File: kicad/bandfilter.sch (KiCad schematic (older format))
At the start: 102 parts, among them J1 Antenna, J2 Rx, J3 Tx, J4 Conn_01x07, J5 Conn_01x07, J6 Antenna, J7 Rx, J8 Tx, T1 40/13T T50-2 (8uH), T2 30/8T T50-2 (4.5uH)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

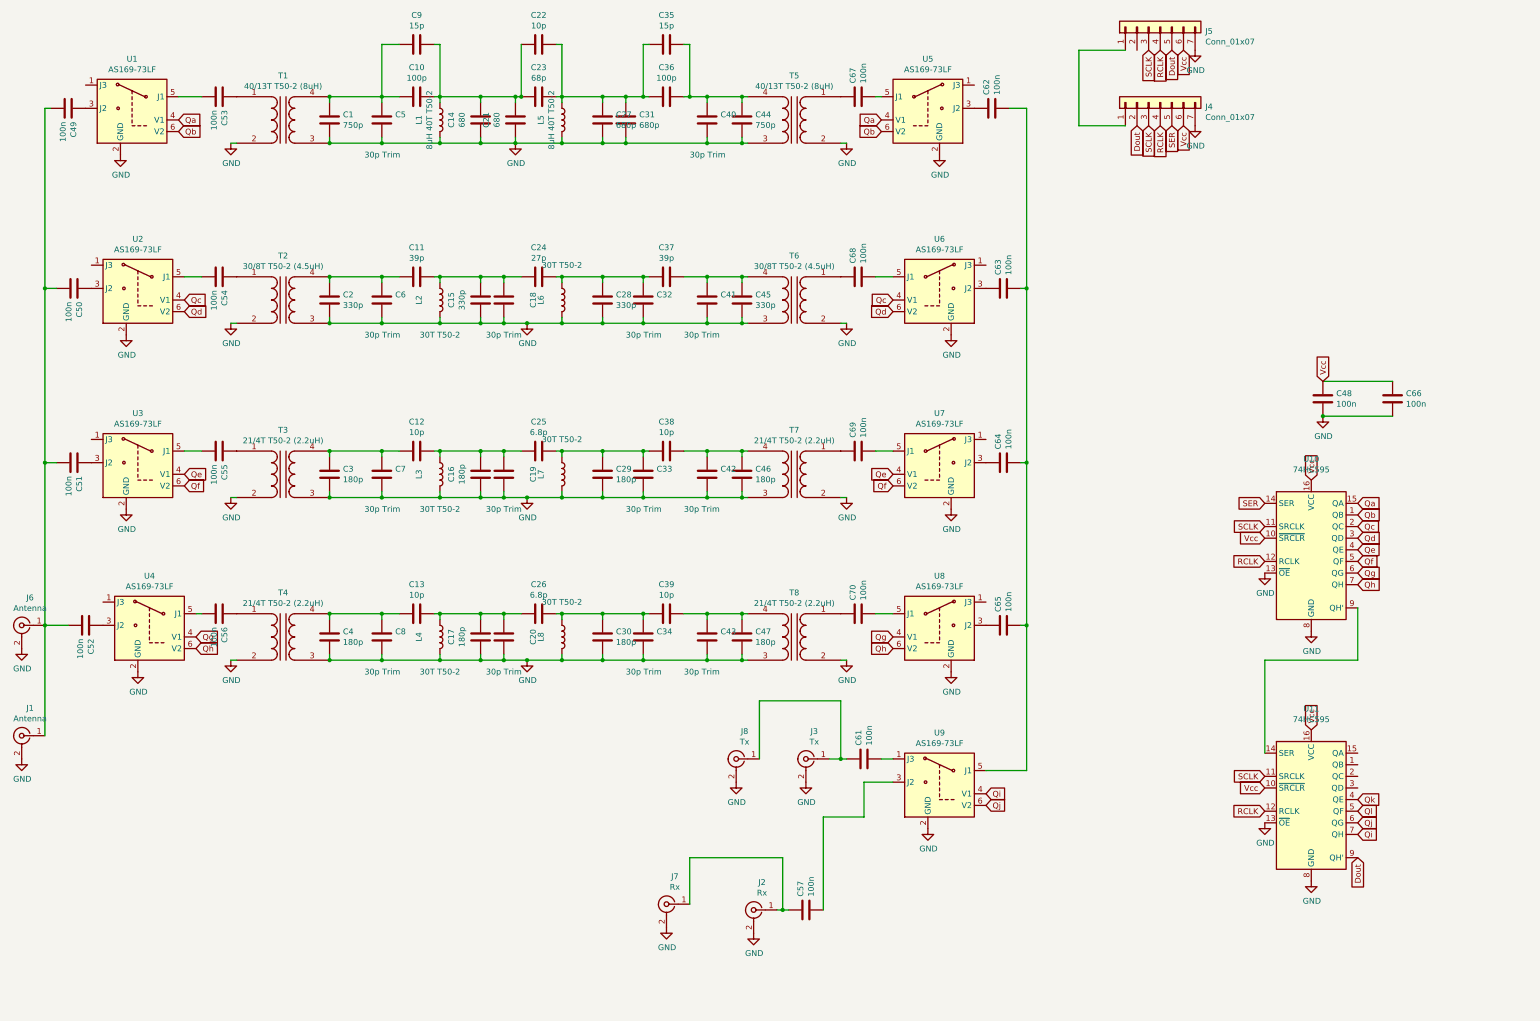
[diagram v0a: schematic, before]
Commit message: I2C version update
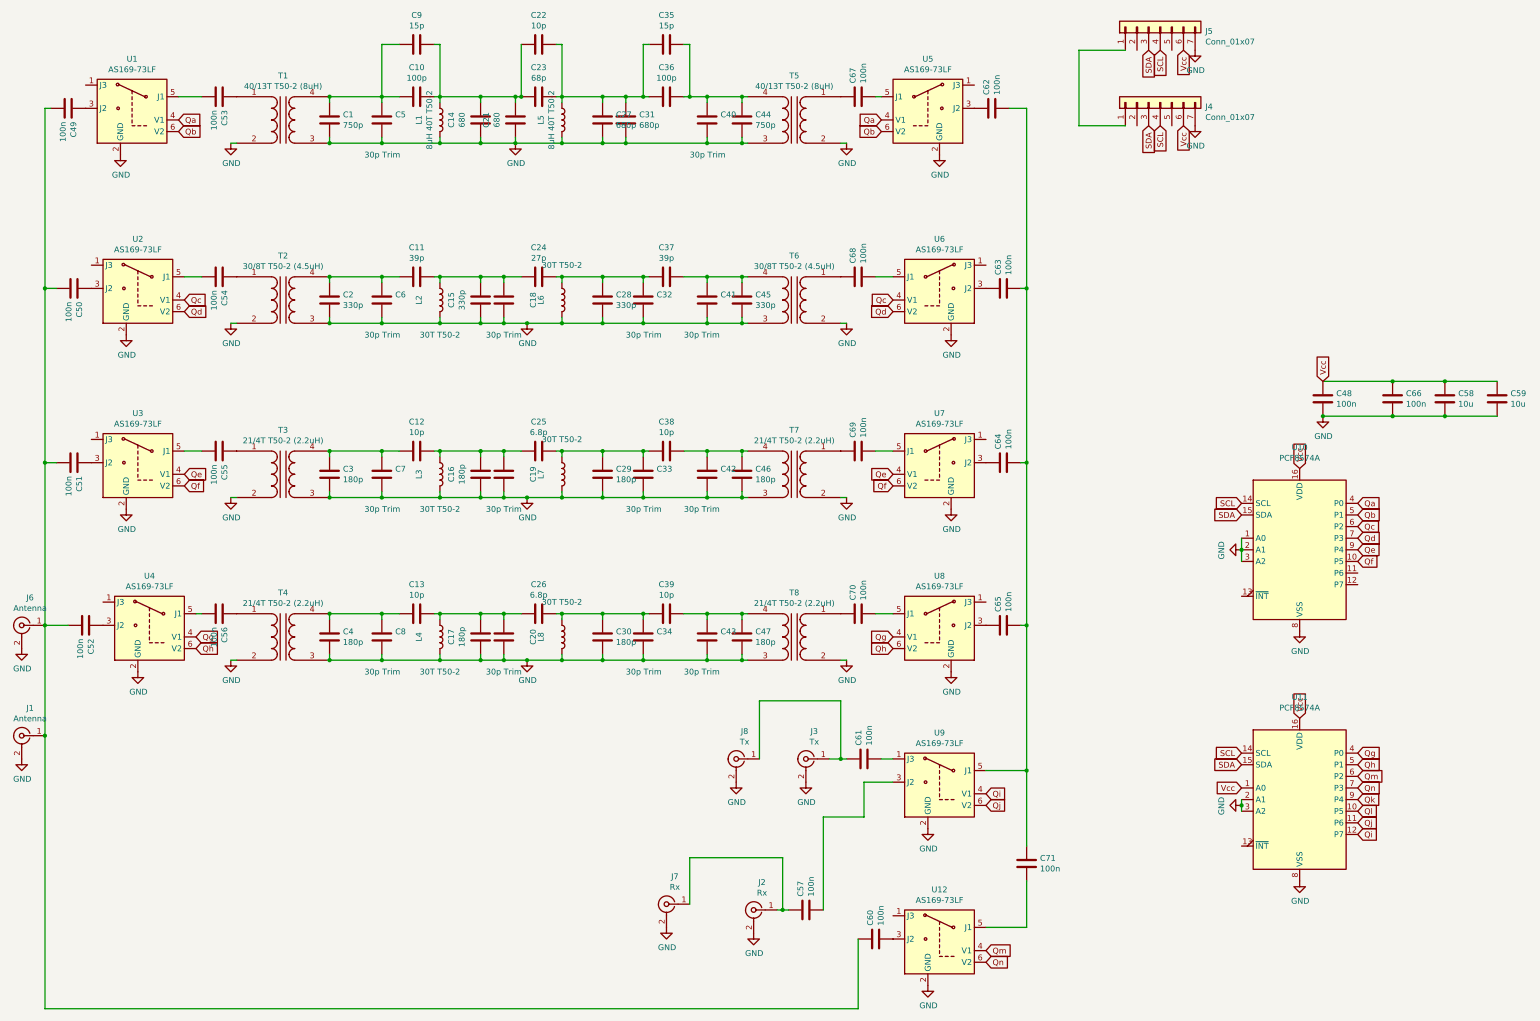
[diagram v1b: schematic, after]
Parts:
- removed U10, U11: 74HC595, Package_DIP:DIP-16_W7.62mm_Socket, symbol 74xx:74HC595
- added C58, C59: 10u, Capacitor_SMD:C_1206_3216Metric_Pad1.42x1.75mm_HandSolder, symbol Device:C
- added C60, C71: 100n, Capacitor_SMD:C_1206_3216Metric_Pad1.42x1.75mm_HandSolder, symbol Device:C
- added U10, U11: PCF8574A, Package_SO:SOP-16_7.5x10.4mm_P1.27mm, symbol Interface_Expansion:PCF8574A
- added U12: AS169-73LF, Package_TO_SOT_SMD:SOT-23-6_Handsoldering, symbol bandfilter-rescue:AS169-73LF-RF_Switch
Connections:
- net GND: now also C58.1, C59.1, U10.1 (A0), U10.2 (A1), U10.3 (A2), U10.8 (VSS), U11.2 (A1), U11.3 (A2), U11.8 (VSS), U12.2 (GND)
- net Qa: now also U10.4 (P0)
- net Qb: now also U10.5 (P1)
- net Qc: now also U10.6 (P2)
- net Qd: now also U10.7 (P3)
- net Qe: now also U10.9 (P4)
- net Qf: now also U10.10 (P5)
- net Qg: now also U11.4 (P0)
- net Qh: now also U11.5 (P1)
- net Qi: now also U11.12 (P7)
- net Qj: now also U11.11 (P6)
- net Qk: now also U11.9 (P4)
- net Ql: now also U11.10 (P5)
- net Vcc: now also C58.2, C59.2, U10.16 (VDD), U11.1 (A0), U11.16 (VDD)
- net at C49.1, C50.1, C51.1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: now also C60.2
- net at C62.1, C63.1, C64.1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: now also C71.2
- net Dout: no longer names the net of J4.2 (Pin_2)
- net Dout: no longer J5.5 (Pin_5)
- net RCLK renamed SCL
- net SCL: now also U10.14 (SCL), U11.14 (SCL)
- net SCLK renamed SDA
- net SDA: now also U10.15 (SDA), U11.15 (SDA)
- net SER: no longer names the net of J4.5 (Pin_5)
- new net: C60.1, U12.3 (J2)
- new net: C71.1, U12.5 (J1)
- new net Qm: U11.6 (P2), U12.4 (V1)
- new net Qn: U11.7 (P3), U12.6 (V2)
